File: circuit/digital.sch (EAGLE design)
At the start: 32 parts, among them IC1 MCP1701-5V, IC2 MCP1700-3.3V, X1 MINI-USB-SCHIELD-32005-301

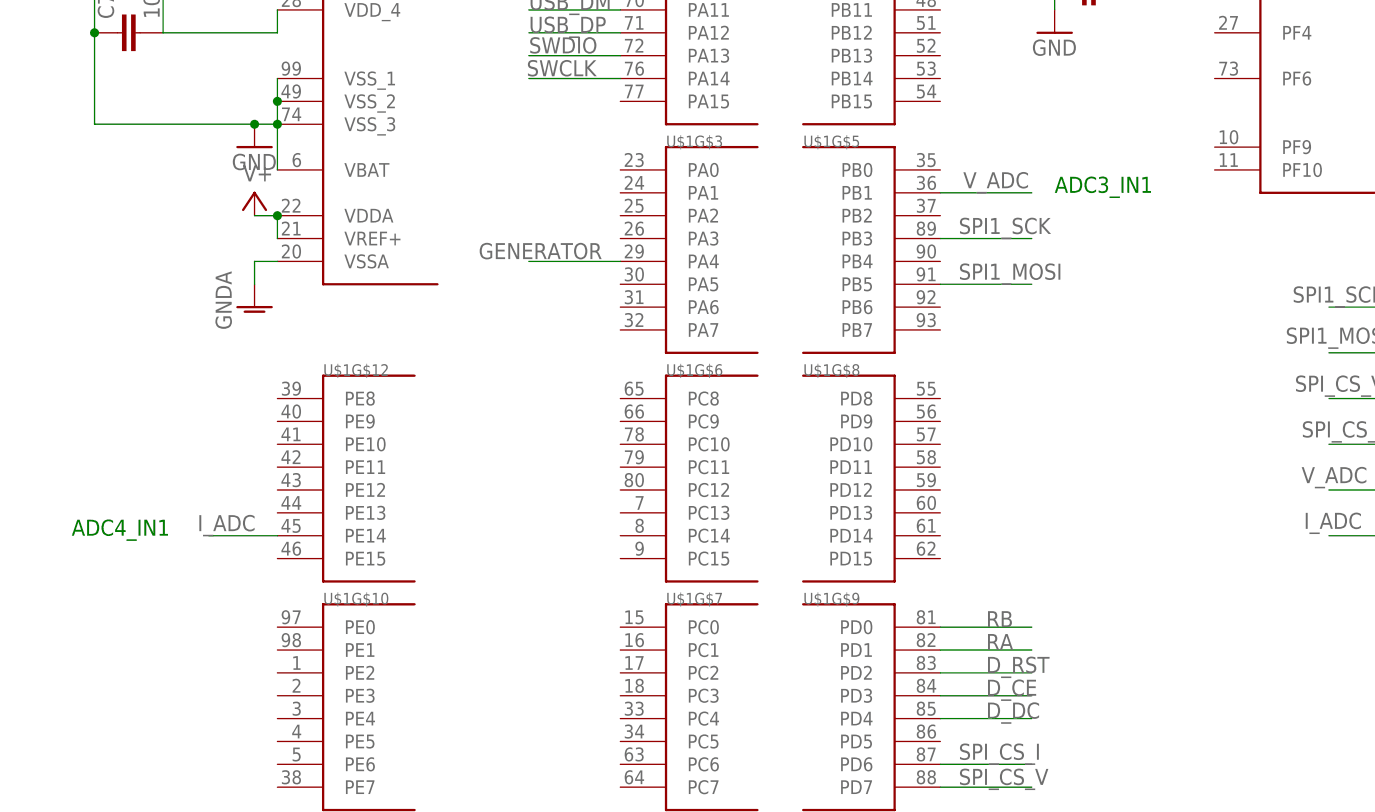
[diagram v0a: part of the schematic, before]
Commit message: - перенесли конденсаторы фильтрующие частоту для ADC на цифровую часть схемы
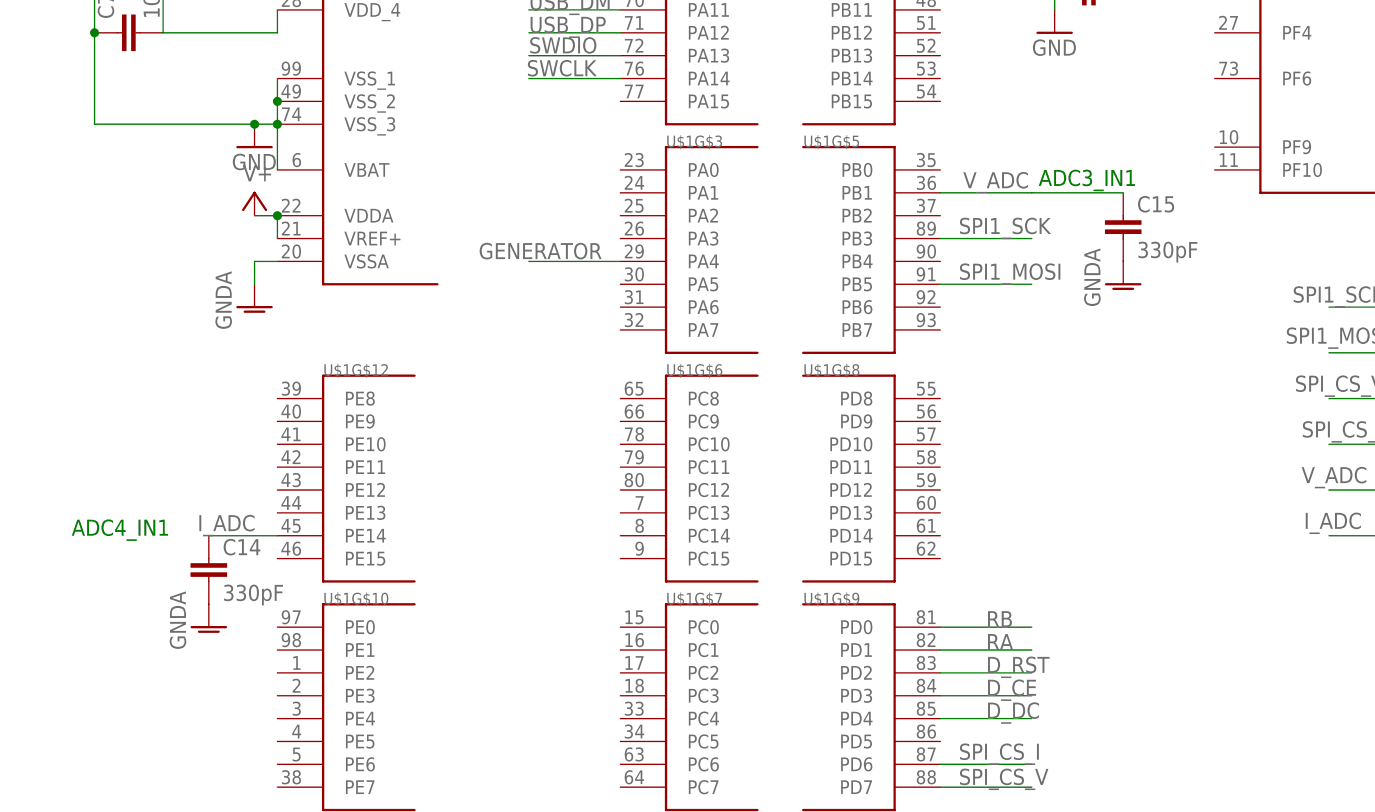
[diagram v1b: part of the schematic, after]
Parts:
- added C14, C15: 330pF, rcl:C-EUC0805
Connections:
- net GNDA: now also C14.2, C15.2
- net I_ADC: now also C14.1
- net V_ADC: now also C15.1
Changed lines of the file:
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@@
 <part name="R5" library="rcl" deviceset="R-EU_" device="R0603" value="22"/>
 <part name="X5" library="con-phoenix-254" deviceset="MPT2" device=""/>
+<part name="C14" library="rcl" deviceset="C-EU" device="C0805" value="330pF"/>
+<part name="GND14" library="supply1" deviceset="GNDA" device=""/>
+<part name="C15" library="rcl" deviceset="C-EU" device="C0805" value="330pF"/>
+<part name="GND15" library="supply1" deviceset="GNDA" device=""/>
 </parts>
 <sheets>
@@
 <plain>
 <text x="-10.16" y="-38.1" size="1.778" layer="91">ADC4_IN1</text>
-<text x="99.06" y="0" size="1.778" layer="91">ADC3_IN1</text>
+<text x="97.282" y="0.762" size="1.778" layer="91">ADC3_IN1</text>
 </plain>
 <instances>
@@
 <instance part="X5" gate="-1" x="81.28" y="71.12"/>
 <instance part="X5" gate="-2" x="81.28" y="66.04"/>
+<instance part="C14" gate="G$1" x="5.08" y="-40.64"/>
+<instance part="GND14" gate="1" x="5.08" y="-48.26"/>
+<instance part="C15" gate="G$1" x="106.68" y="-2.54"/>
+<instance part="GND15" gate="1" x="106.68" y="-10.16"/>
 </instances>
 <busses>
@@
 <wire x1="101.6" y1="91.44" x2="104.14" y2="91.44" width="0.1524" layer="91"/>
 </segment>
+<segment>
+<pinref part="C14" gate="G$1" pin="2"/>
+<pinref part="GND14" gate="1" pin="GNDA"/>
+</segment>
+<segment>
+<pinref part="C15" gate="G$1" pin="2"/>
+<pinref part="GND15" gate="1" pin="GNDA"/>
+</segment>
 </net>
 <net name="V_ADC" class="0">
@@
 <wire x1="86.36" y1="0" x2="96.52" y2="0" width="0.1524" layer="91"/>
 <label x="88.9" y="0.508" size="1.778" layer="95"/>
+<pinref part="C15" gate="G$1" pin="1"/>
+<wire x1="96.52" y1="0" x2="106.68" y2="0" width="0.1524" layer="91"/>
 </segment>
 <segment>
@@
 <wire x1="12.7" y1="-38.1" x2="5.08" y2="-38.1" width="0.1524" layer="91"/>
 <label x="3.81" y="-37.592" size="1.778" layer="95"/>
-</segment>
-<segment>
+<pinref part="C14" gate="G$1" pin="1"/>
+</segment>
+<segment>

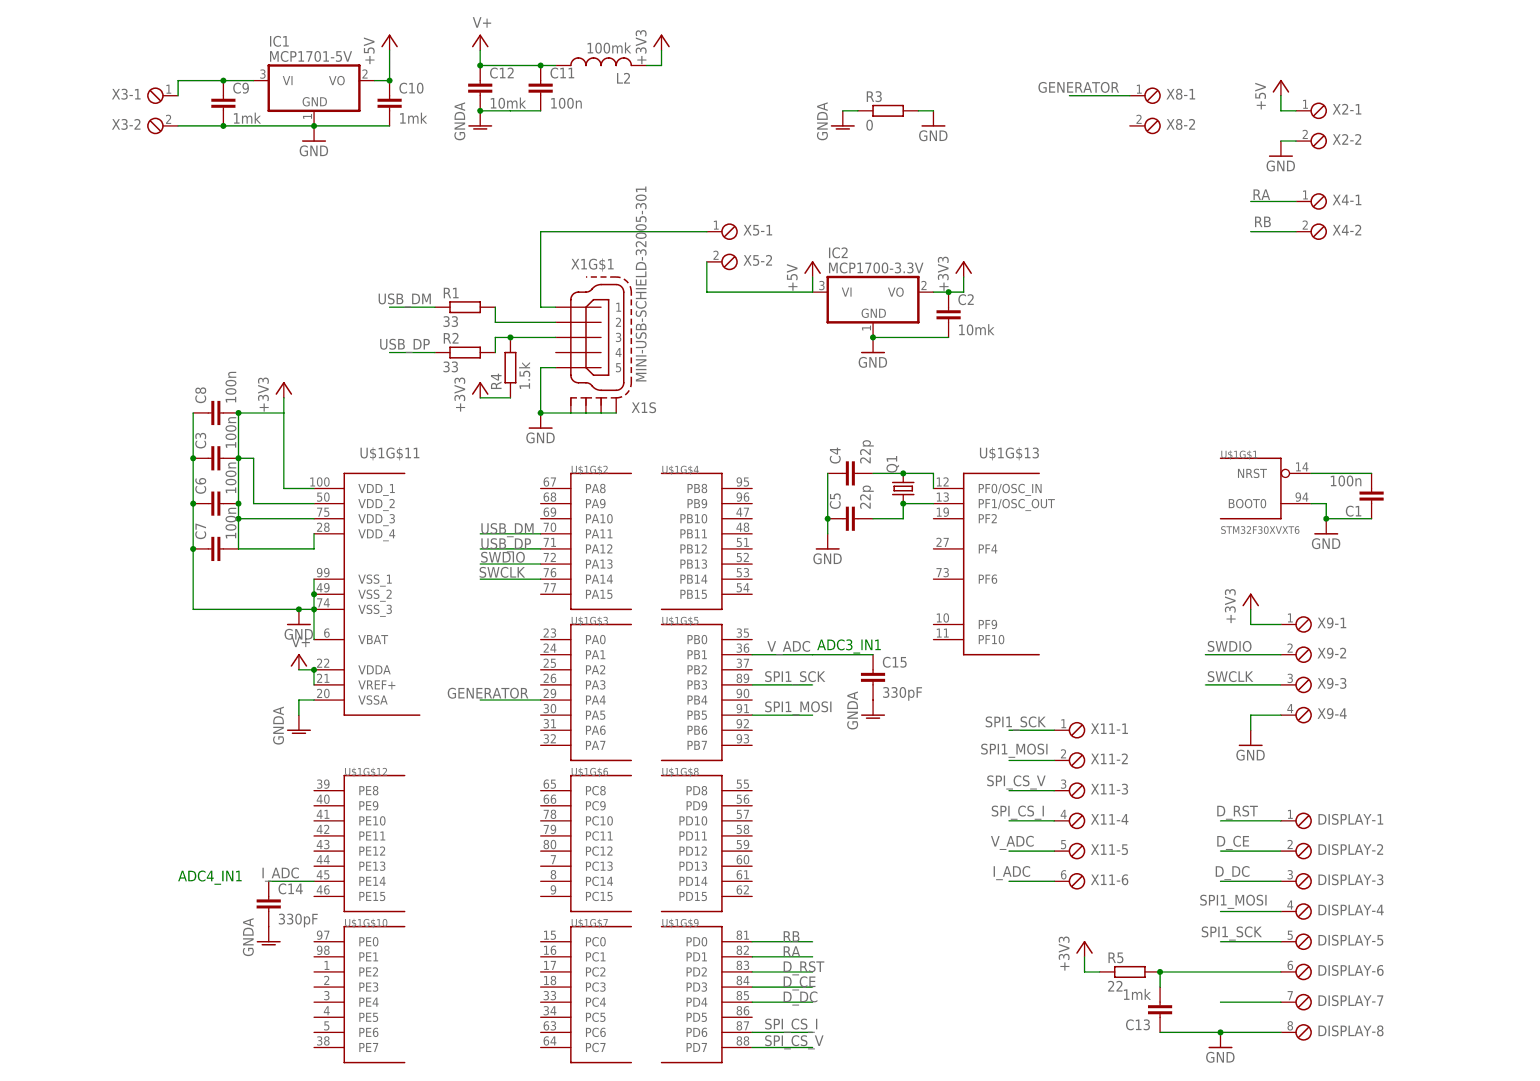
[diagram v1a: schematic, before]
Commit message: - совместили северные контакты - добавили RC цепочки между первым и вторым каскадом усиления - добавили неподключеный коннектор, чтобы было на чем держаться дисплею
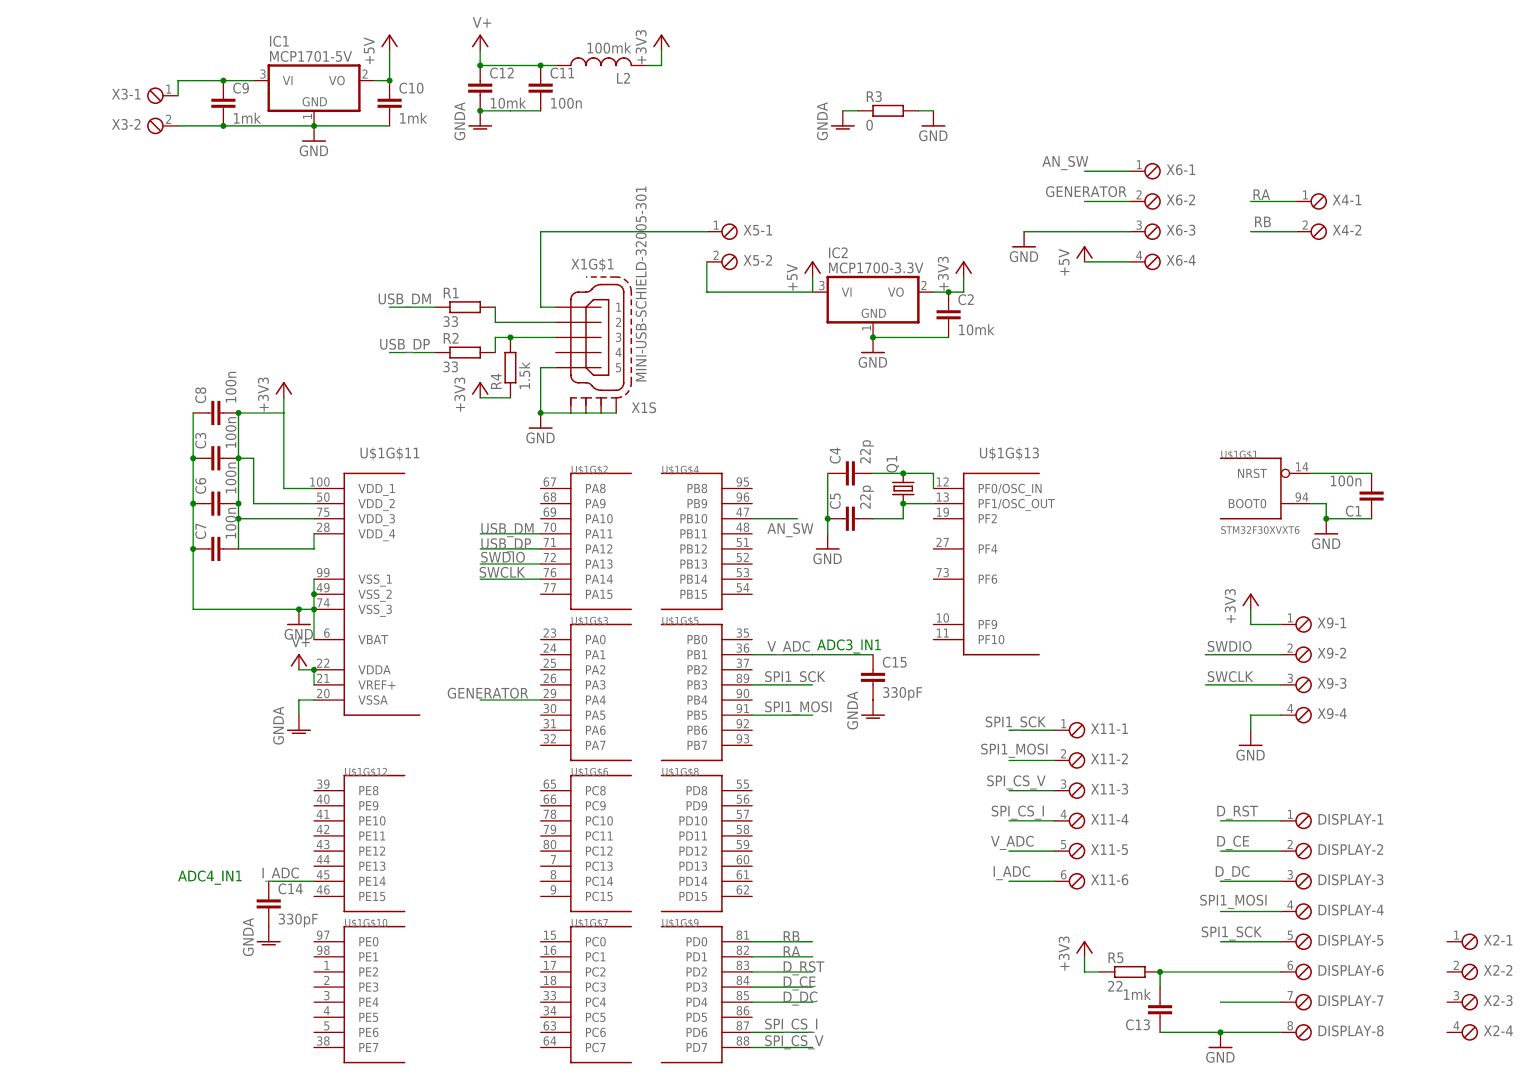
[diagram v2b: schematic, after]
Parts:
- removed X8: (no value), con-phoenix-254:MPT2
- added X6: (no value), con-phoenix-254:MPT4
- X2: device con-phoenix-254:MPT2 -> con-phoenix-254:MPT4
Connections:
- new net AN_SW: U$1G$4.PB10, X6-1.1
- net +5V: now also X6-4.1; no longer X2-1.1
- net GENERATOR: now also X6-2.1; no longer X8-1.1
- net GND: now also X6-3.1; no longer X2-2.1
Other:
- moved on the sheet: X2-1, X2-2
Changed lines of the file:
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@@
 <part name="C12" library="rcl" deviceset="C-EU" device="C0805" value="10mk"/>
 <part name="GND10" library="supply1" deviceset="GNDA" device=""/>
-<part name="X2" library="con-phoenix-254" deviceset="MPT2" device=""/>
 <part name="X4" library="con-phoenix-254" deviceset="MPT2" device=""/>
-<part name="P+7" library="supply1" deviceset="+5V" device=""/>
-<part name="X8" library="con-phoenix-254" deviceset="MPT2" device=""/>
 <part name="SUPPLY1" library="supply2" deviceset="V+" device=""/>
 <part name="IC1" library="linear" deviceset="MCP1703" device="CB" value="MCP1701-5V"/>
@@
 <part name="C1" library="rcl" deviceset="C-EU" device="C0603" value="100n"/>
 <part name="GND1" library="supply1" deviceset="GND" device=""/>
-<part name="GND2" library="supply1" deviceset="GND" device=""/>
 <part name="GND3" library="supply1" deviceset="GND" device=""/>
 <part name="GND4" library="supply1" deviceset="GND" device=""/>
@@
 <part name="C15" library="rcl" deviceset="C-EU" device="C0805" value="330pF"/>
 <part name="GND15" library="supply1" deviceset="GNDA" device=""/>
+<part name="X6" library="con-phoenix-254" deviceset="MPT4" device=""/>
+<part name="P+3" library="supply1" deviceset="+5V" device=""/>
+<part name="GND16" library="supply1" deviceset="GND" device=""/>
+<part name="X2" library="con-phoenix-254" deviceset="MPT4" device=""/>
 </parts>
 <sheets>
@@
 <instance part="C12" gate="G$1" x="40.64" y="96.52"/>
 <instance part="GND10" gate="1" x="40.64" y="88.9"/>
-<instance part="X2" gate="-1" x="180.34" y="91.44"/>
-<instance part="X2" gate="-2" x="180.34" y="86.36"/>
 <instance part="X4" gate="-1" x="180.34" y="76.2"/>
 <instance part="X4" gate="-2" x="180.34" y="71.12"/>
-<instance part="P+7" gate="1" x="175.26" y="96.52"/>
-<instance part="X8" gate="-1" x="152.4" y="93.98"/>
-<instance part="X8" gate="-2" x="152.4" y="88.9"/>
 <instance part="SUPPLY1" gate="1" x="40.64" y="104.14"/>
 <instance part="IC1" gate="G$1" x="12.7" y="96.52"/>
@@
 <instance part="C1" gate="G$1" x="190.5" y="25.4" rot="R180"/>
 <instance part="GND1" gate="1" x="182.88" y="20.32"/>
-<instance part="GND2" gate="1" x="175.26" y="83.82"/>
 <instance part="GND3" gate="1" x="50.8" y="38.1"/>
 <instance part="GND4" gate="1" x="106.68" y="50.8"/>
@@
 <instance part="C15" gate="G$1" x="106.68" y="-2.54"/>
 <instance part="GND15" gate="1" x="106.68" y="-10.16"/>
+<instance part="X6" gate="-1" x="152.4" y="81.28"/>
+<instance part="X6" gate="-2" x="152.4" y="76.2"/>
+<instance part="X6" gate="-3" x="152.4" y="71.12"/>
+<instance part="X6" gate="-4" x="152.4" y="66.04"/>
+<instance part="P+3" gate="1" x="142.24" y="68.58"/>
+<instance part="GND16" gate="1" x="132.08" y="68.58"/>
+<instance part="X2" gate="-1" x="205.74" y="-48.26"/>
+<instance part="X2" gate="-2" x="205.74" y="-53.34"/>
+<instance part="X2" gate="-3" x="205.74" y="-58.42"/>
+<instance part="X2" gate="-4" x="205.74" y="-63.5"/>
 </instances>
 <busses>
@@
 <net name="GENERATOR" class="0">
 <segment>
-<pinref part="X8" gate="-1" pin="1"/>
-<wire x1="149.86" y1="93.98" x2="139.7" y2="93.98" width="0.1524" layer="91"/>
-<label x="134.366" y="94.488" size="1.778" layer="95"/>
-</segment>
-<segment>
 <pinref part="U$1" gate="G$3" pin="PA4"/>
 <wire x1="50.8" y1="-7.62" x2="40.64" y2="-7.62" width="0.1524" layer="91"/>
 <label x="35.052" y="-7.366" size="1.778" layer="95"/>
 </segment>
+<segment>
+<pinref part="X6" gate="-2" pin="1"/>
+<wire x1="149.86" y1="76.2" x2="142.24" y2="76.2" width="0.1524" layer="91"/>
+<label x="135.636" y="76.962" size="1.778" layer="95"/>
+</segment>
 </net>
 <net name="+5V" class="0">
-<segment>
-<pinref part="X2" gate="-1" pin="1"/>
-<pinref part="P+7" gate="1" pin="+5V"/>
-<wire x1="177.8" y1="91.44" x2="175.26" y2="91.44" width="0.1524" layer="91"/>
-<wire x1="175.26" y1="91.44" x2="175.26" y2="93.98" width="0.1524" layer="91"/>
-</segment>
 <segment>
 <pinref part="P+1" gate="1" pin="+5V"/>
@@
 <wire x1="25.4" y1="96.52" x2="25.4" y2="101.6" width="0.1524" layer="91"/>
 <junction x="25.4" y="96.52"/>
+</segment>
+<segment>
+<pinref part="X6" gate="-4" pin="1"/>
+<wire x1="149.86" y1="66.04" x2="142.24" y2="66.04" width="0.1524" layer="91"/>
+<pinref part="P+3" gate="1" pin="+5V"/>
 </segment>
 </net>
@@
 <wire x1="190.5" y1="22.86" x2="182.88" y2="22.86" width="0.1524" layer="91"/>
 <junction x="182.88" y="22.86"/>
-</segment>
-<segment>
-<pinref part="X2" gate="-2" pin="1"/>
-<wire x1="177.8" y1="86.36" x2="175.26" y2="86.36" width="0.1524" layer="91"/>
-<pinref part="GND2" gate="1" pin="GND"/>
 </segment>
 <segment>
@@
 <wire x1="165.1" y1="-63.5" x2="154.94" y2="-63.5" width="0.1524" layer="91"/>
 <junction x="165.1" y="-63.5"/>
+</segment>
+<segment>
+<pinref part="X6" gate="-3" pin="1"/>
+<wire x1="149.86" y1="71.12" x2="142.24" y2="71.12" width="0.1524" layer="91"/>
+<pinref part="GND16" gate="1" pin="GND"/>
+<wire x1="132.08" y1="71.12" x2="142.24" y2="71.12" width="0.1524" layer="91"/>
 </segment>
 </net>
@@
 </segment>
 </net>
+<net name="AN_SW" class="0">
+<segment>
+<pinref part="X6" gate="-1" pin="1"/>
+<wire x1="149.86" y1="81.28" x2="142.24" y2="81.28" width="0.1524" layer="91"/>
+<label x="135.128" y="82.042" size="1.778" layer="95"/>
+</segment>
+<segment>
+<pinref part="U$1" gate="G$4" pin="PB10"/>
+<wire x1="86.36" y1="22.86" x2="93.98" y2="22.86" width="0.1524" layer="91"/>
+<label x="88.9" y="20.32" size="1.778" layer="95"/>
+</segment>
+</net>
